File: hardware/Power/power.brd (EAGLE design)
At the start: 71 x 71 mm, 42 parts, among them IC1 ACS712ELCTR-05B-T, IC2 LM358_SOIC, Q1 PNP, T1 ZMPT101B, X1 057-006-1

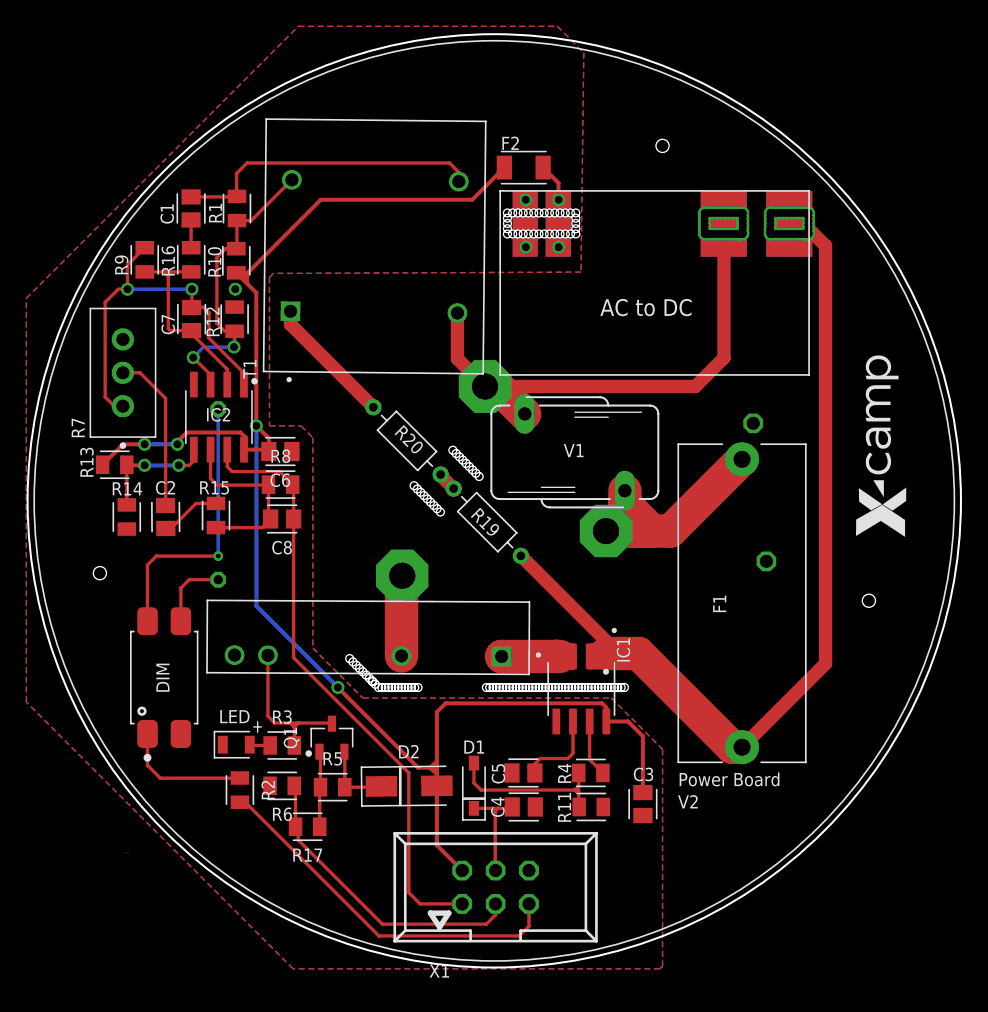
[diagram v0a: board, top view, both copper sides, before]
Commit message: fix : 2 layer pcb, dim pin terhalang
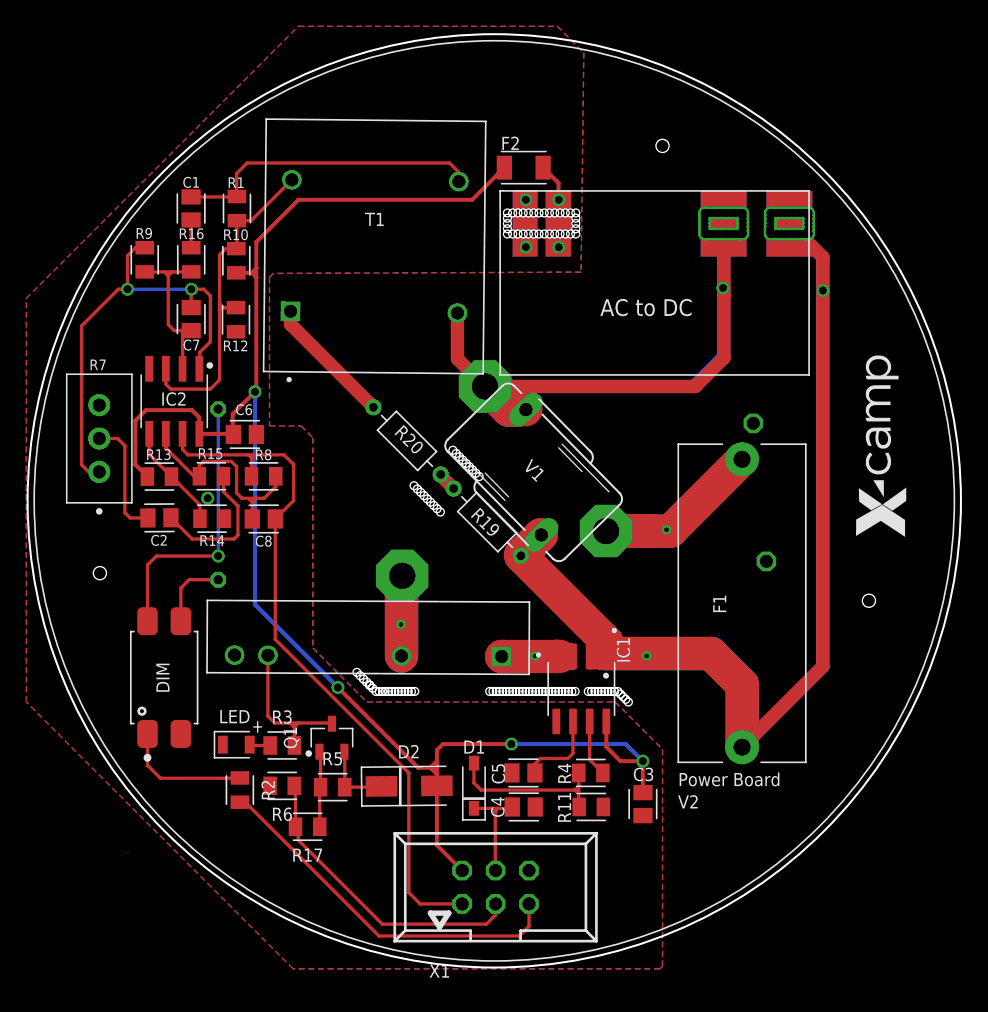
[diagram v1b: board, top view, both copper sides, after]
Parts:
- moved R14 6.49 mm to (-21.5, -1.36), turned to 180 degrees
- moved R7 5.31 mm to (-30.0, 2.20)
- moved IC2 3.61 mm to (-24.3, 7.57)
- moved R13 3.52 mm to (-25.5, 1.85)
- moved V1 3.48 mm to (2.99, 2.17), turned to 44.5 degrees
- moved R15 3.00 mm to (-21.5, 1.87), turned to 180 degrees
- moved C6 3.00 mm to (-19.0, 5.05)
- moved R8 1.44 mm to (-17.5, 1.86), turned to 180 degrees
- moved C8 1.40 mm to (-17.5, -1.38)
- moved C2 0.48 mm to (-25.5, -1.29), turned to 0.4 degrees
- moved R12 0.11 mm to (-19.6, 13.8), turned to 90 degrees
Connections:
- net L: no longer V1.1
- net L_FUSE: now also V1.1
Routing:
- net L_FUSE: track 73.9 -> 149.6 mm, vias 0 -> 2
- net N: track 39.9 -> 73.3 mm, vias 0 -> 1
- net ADC_VOLTAGE: track 46.1 -> 54.0 mm
- net N$17: track 4.61 -> 10.8 mm
- net OUT-A: track 29.0 -> 34.7 mm
- net V: track 7.19 -> 12.7 mm, vias 0 -> 1
- net L: track 23.9 -> 27.9 mm, vias 0 -> 1
- net POS-A: track 23.2 -> 27.0 mm, vias 2 -> 0
- net N$16: track 14.0 -> 17.6 mm
- net N$18: track 12.2 -> 9.19 mm
- net N$6: track 15.5 -> 13.5 mm
- net POS-B: track 9.15 -> 8.05 mm, vias 2 -> 0
- net L_OUT: vias 0 -> 1

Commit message: checkpoint 21/05
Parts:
- AC-DC: value (none) -> HI-LINKAC-DC_3.5W(PTH); device XLKM#4:AC-DC_3.5W(VER) -> XLKM#4:AC-DC_3.5W(PTH)
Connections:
- net F_5V: now also AC-DC.5V; no longer AC-DC.5V_B, AC-DC.5V_T
- net GND: now also AC-DC.GND; no longer AC-DC.GND_B, AC-DC.GND_T
- net L_FUSE: now also AC-DC.L; no longer AC-DC.L_B, AC-DC.L_T
- net N: now also AC-DC.N; no longer AC-DC.N_B, AC-DC.N_T
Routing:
- net F_5V: track 10.2 -> 6.97 mm, vias 2 -> 3
- net L_FUSE: track 149.6 -> 151.6 mm, vias 2 -> 4
- net N: track 73.3 -> 75.3 mm, vias 1 -> 3
- net N$1: track 23.5 -> 22.7 mm
- net 5V: track 123.2 -> 123.9 mm
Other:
- outline, holes or cut-outs redrawn

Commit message: feat : react to esp32 script
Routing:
- net L_FUSE: track 151.6 -> 145.5 mm, vias 4 -> 2
- net L_OUT: track 9.46 -> 13.9 mm
- net N: track 75.3 -> 73.2 mm, vias 3 -> 1
- net F_5V: track 6.97 -> 7.14 mm, vias 3 -> 1
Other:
- outline, holes or cut-outs redrawn
- board text added: "V2.5"
- board text removed: "V2"
